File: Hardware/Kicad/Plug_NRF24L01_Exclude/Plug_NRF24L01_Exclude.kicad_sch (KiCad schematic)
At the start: 38 parts, among them J1 Conn_01x07_Socket, J2 Conn_01x08_Socket, J2 Conn_02x07_Odd_Even, Q1 2N7002, Q2 2N7002, Q3 2N7002, SW2 SW_SPST, U2 MIC5219-3.3YMM, U3 STM32L412KBTx

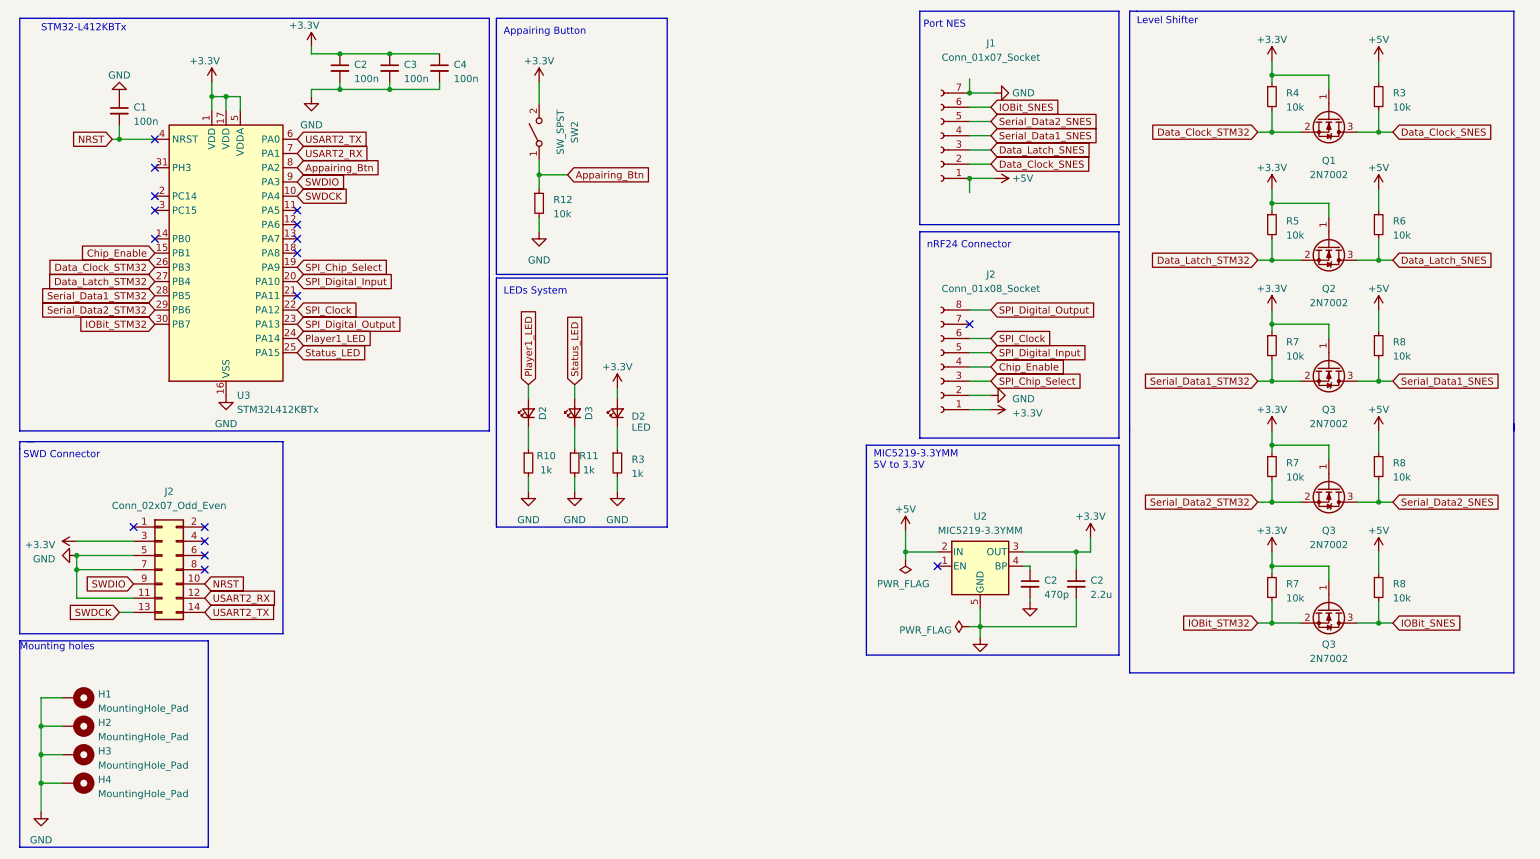
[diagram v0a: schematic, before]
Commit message: Updated Plug_NRF24L01_Exclude (V2.0) - Schematic (NRF24 Connector) - PCB (Capacitor)
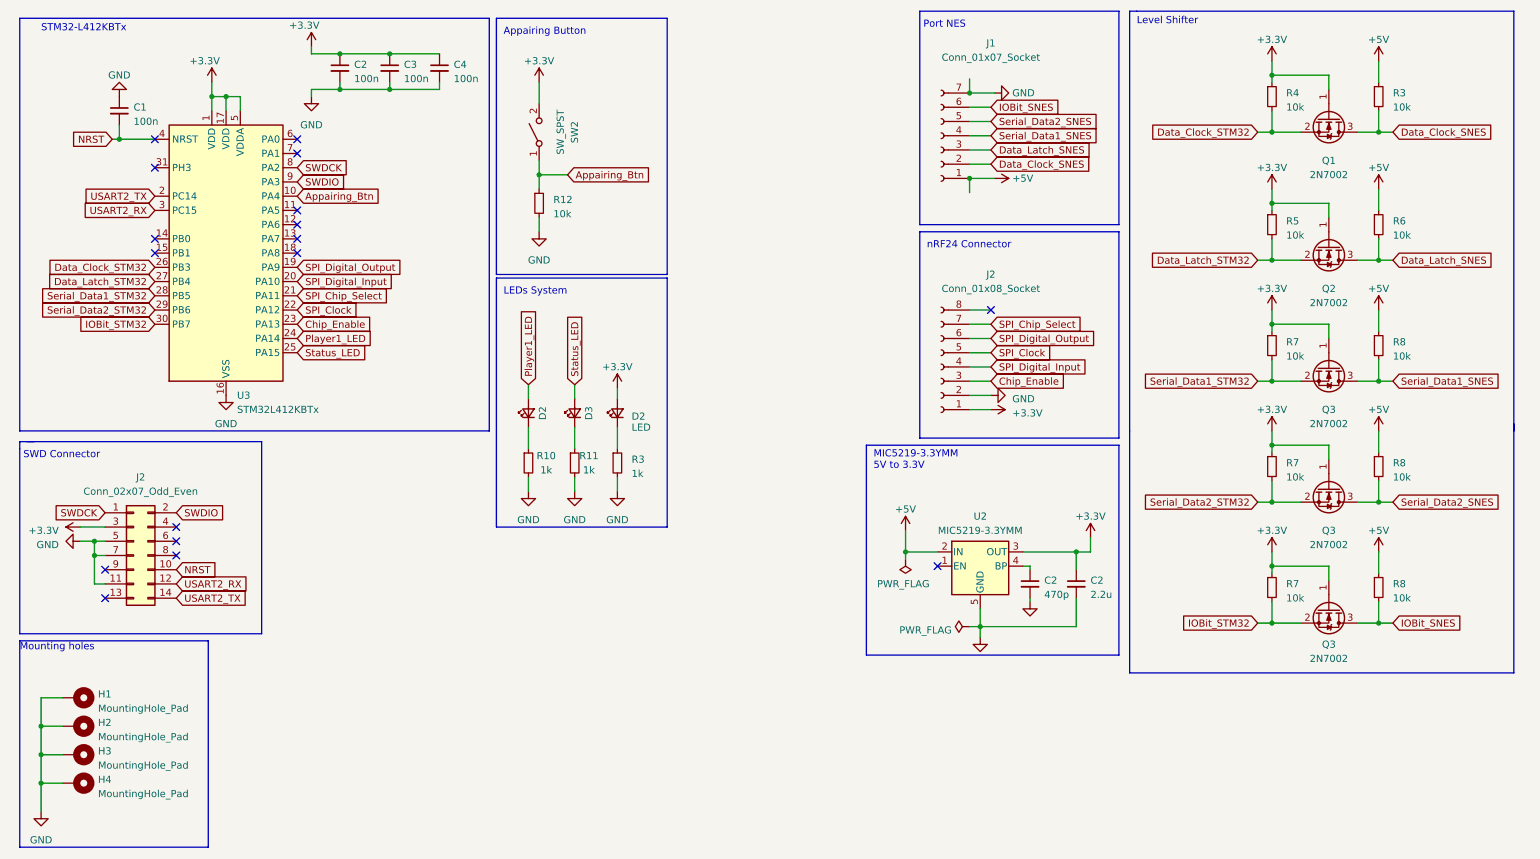
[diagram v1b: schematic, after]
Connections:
- net Appairing_Btn: now also U3.10 (PA4); no longer U3.8 (PA2)
- net Chip_Enable: now also J2.3 (Pin_3), U3.23 (PA13); no longer J2.4 (Pin_4), U3.15 (PB1)
- net SPI_Chip_Select: now also J2.7 (Pin_7), U3.21 (PA11); no longer J2.3 (Pin_3), U3.19 (PA9)
- net SPI_Clock: now also J2.5 (Pin_5); no longer J2.6 (Pin_6)
- net SPI_Digital_Input: now also J2.4 (Pin_4); no longer J2.5 (Pin_5)
- net SPI_Digital_Output: now also J2.6 (Pin_6), U3.19 (PA9); no longer J2.8 (Pin_8), U3.23 (PA13)
- net SWDCK: now also J2.1 (Pin_1), U3.8 (PA2); no longer J2.13 (Pin_13), U3.10 (PA4)
- net SWDIO: now also J2.2 (Pin_2); no longer J2.9 (Pin_9)
- net USART2_RX: now also U3.3 (PC15); no longer U3.7 (PA1)
- net USART2_TX: now also U3.2 (PC14); no longer U3.6 (PA0)
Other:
- moved on the sheet: J2

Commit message: Added a capacitor of 10u for the power of the STM32 on the schematics of the plugs
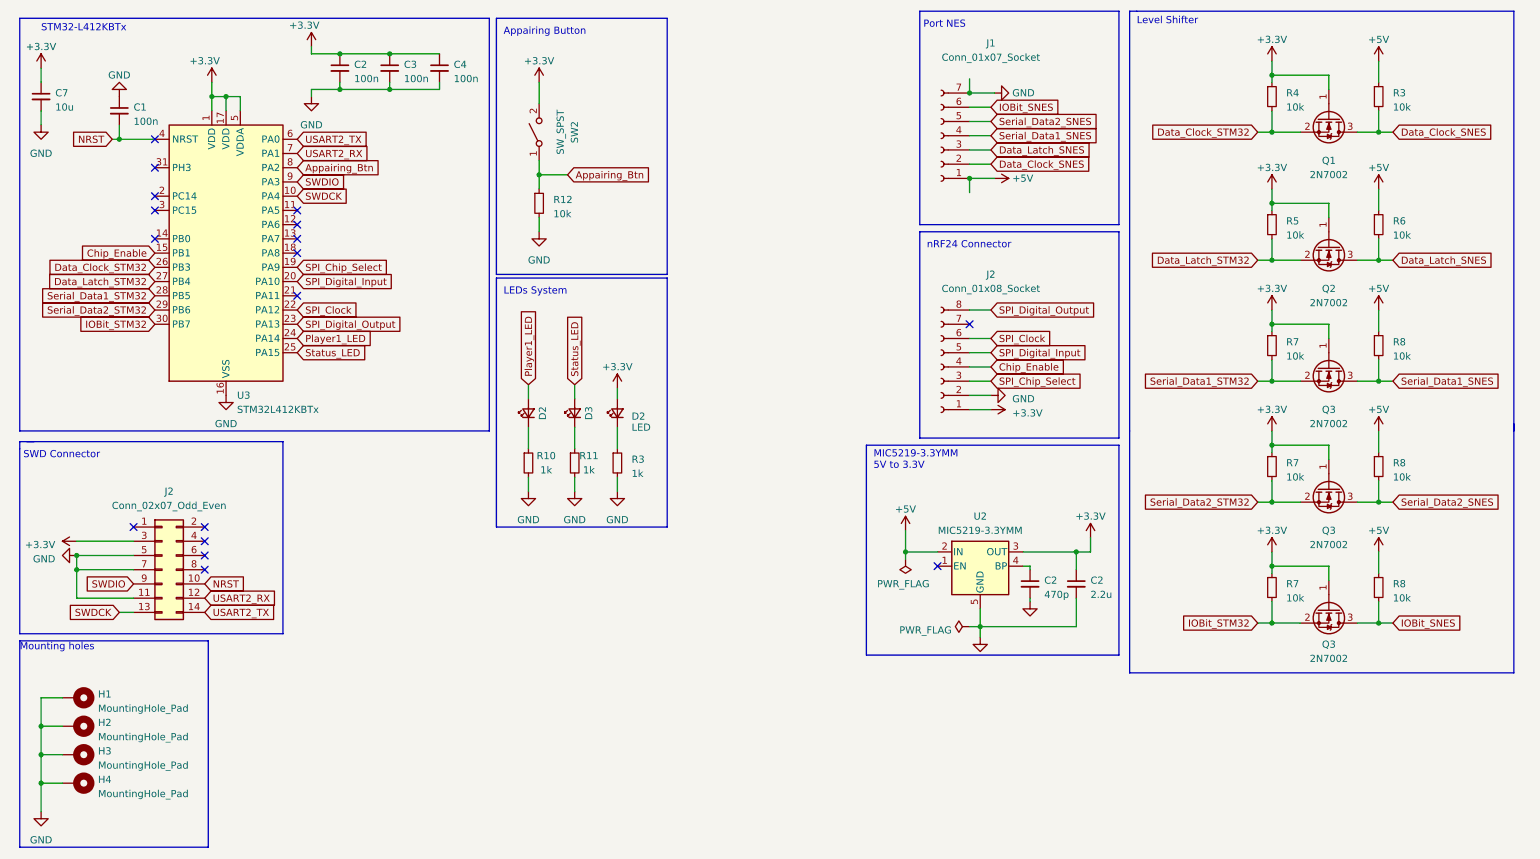
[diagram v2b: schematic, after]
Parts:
- added C7: 10u, Capacitor_SMD:C_0603_1608Metric_Pad1.08x0.95mm_HandSolder, symbol Device:C_Small
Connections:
- net +3.3V: now also C7.1
- net Appairing_Btn: now also U3.8 (PA2); no longer U3.10 (PA4)
- net Chip_Enable: now also J2.4 (Pin_4), U3.15 (PB1); no longer J2.3 (Pin_3), U3.23 (PA13)
- net GND: now also C7.2
- net SPI_Chip_Select: now also J2.3 (Pin_3), U3.19 (PA9); no longer J2.7 (Pin_7), U3.21 (PA11)
- net SPI_Clock: now also J2.6 (Pin_6); no longer J2.5 (Pin_5)
- net SPI_Digital_Input: now also J2.5 (Pin_5); no longer J2.4 (Pin_4)
- net SPI_Digital_Output: now also J2.8 (Pin_8), U3.23 (PA13); no longer J2.6 (Pin_6), U3.19 (PA9)
- net SWDCK: now also J2.13 (Pin_13), U3.10 (PA4); no longer J2.1 (Pin_1), U3.8 (PA2)
- net SWDIO: now also J2.9 (Pin_9); no longer J2.2 (Pin_2)
- net USART2_RX: now also U3.7 (PA1); no longer U3.3 (PC15)
- net USART2_TX: now also U3.6 (PA0); no longer U3.2 (PC14)
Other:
- moved on the sheet: J2

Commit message: Updated Plug_NRF24L01_Exclude (V2.1) - Schematic & PCB (Added 10μ Capacitor)
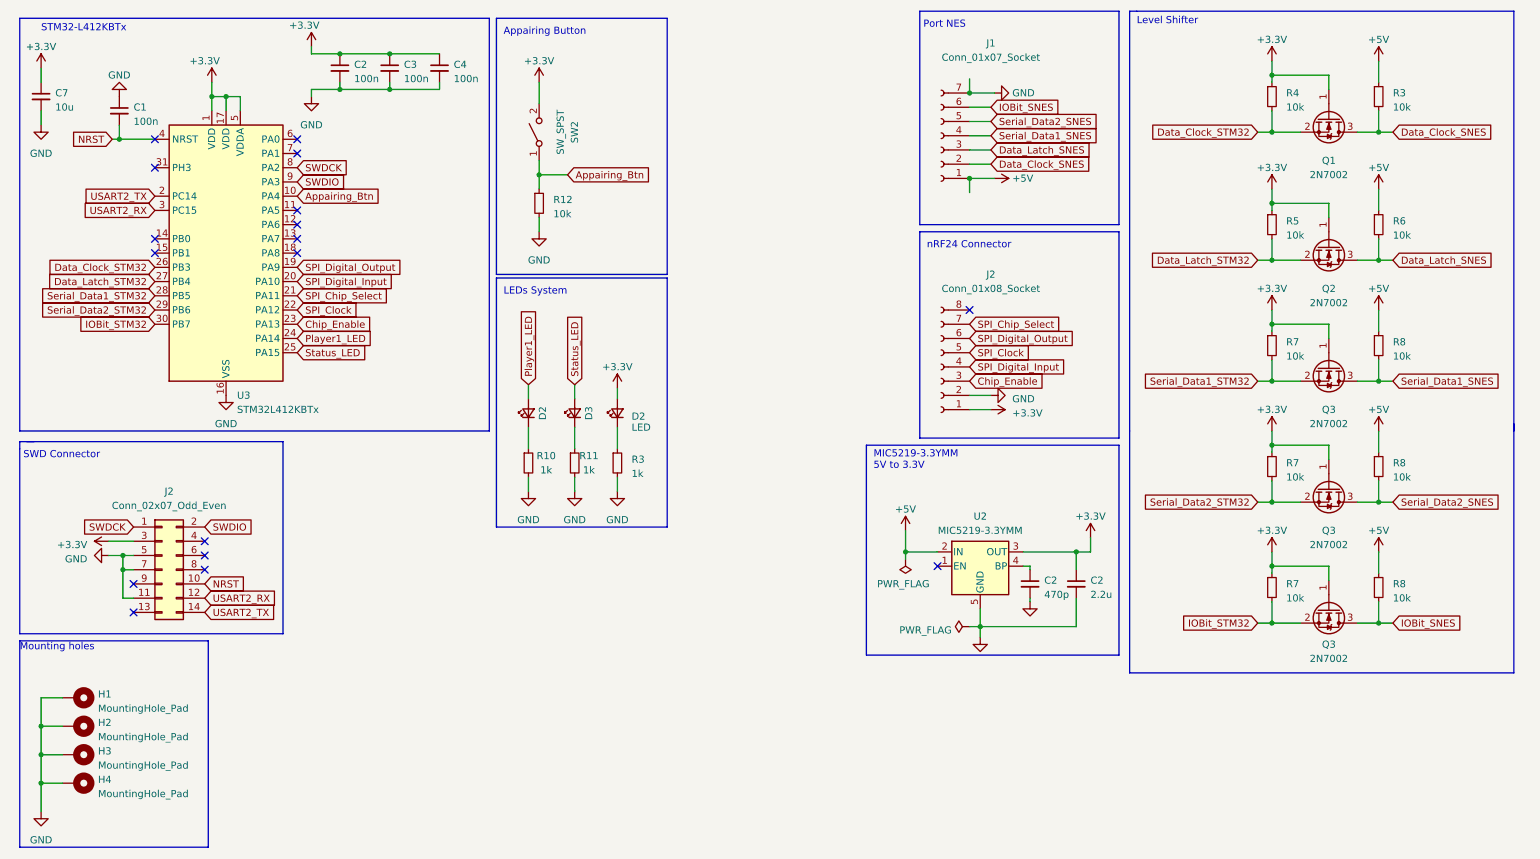
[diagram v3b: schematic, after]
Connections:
- net Appairing_Btn: now also U3.10 (PA4); no longer U3.8 (PA2)
- net Chip_Enable: now also J2.3 (Pin_3), U3.23 (PA13); no longer J2.4 (Pin_4), U3.15 (PB1)
- net SPI_Chip_Select: now also J2.7 (Pin_7), U3.21 (PA11); no longer J2.3 (Pin_3), U3.19 (PA9)
- net SPI_Clock: now also J2.5 (Pin_5); no longer J2.6 (Pin_6)
- net SPI_Digital_Input: now also J2.4 (Pin_4); no longer J2.5 (Pin_5)
- net SPI_Digital_Output: now also J2.6 (Pin_6), U3.19 (PA9); no longer J2.8 (Pin_8), U3.23 (PA13)
- net SWDCK: now also J2.1 (Pin_1), U3.8 (PA2); no longer J2.13 (Pin_13), U3.10 (PA4)
- net SWDIO: now also J2.2 (Pin_2); no longer J2.9 (Pin_9)
- net USART2_RX: now also U3.3 (PC15); no longer U3.7 (PA1)
- net USART2_TX: now also U3.2 (PC14); no longer U3.6 (PA0)
